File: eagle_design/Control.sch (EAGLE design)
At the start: 8 parts

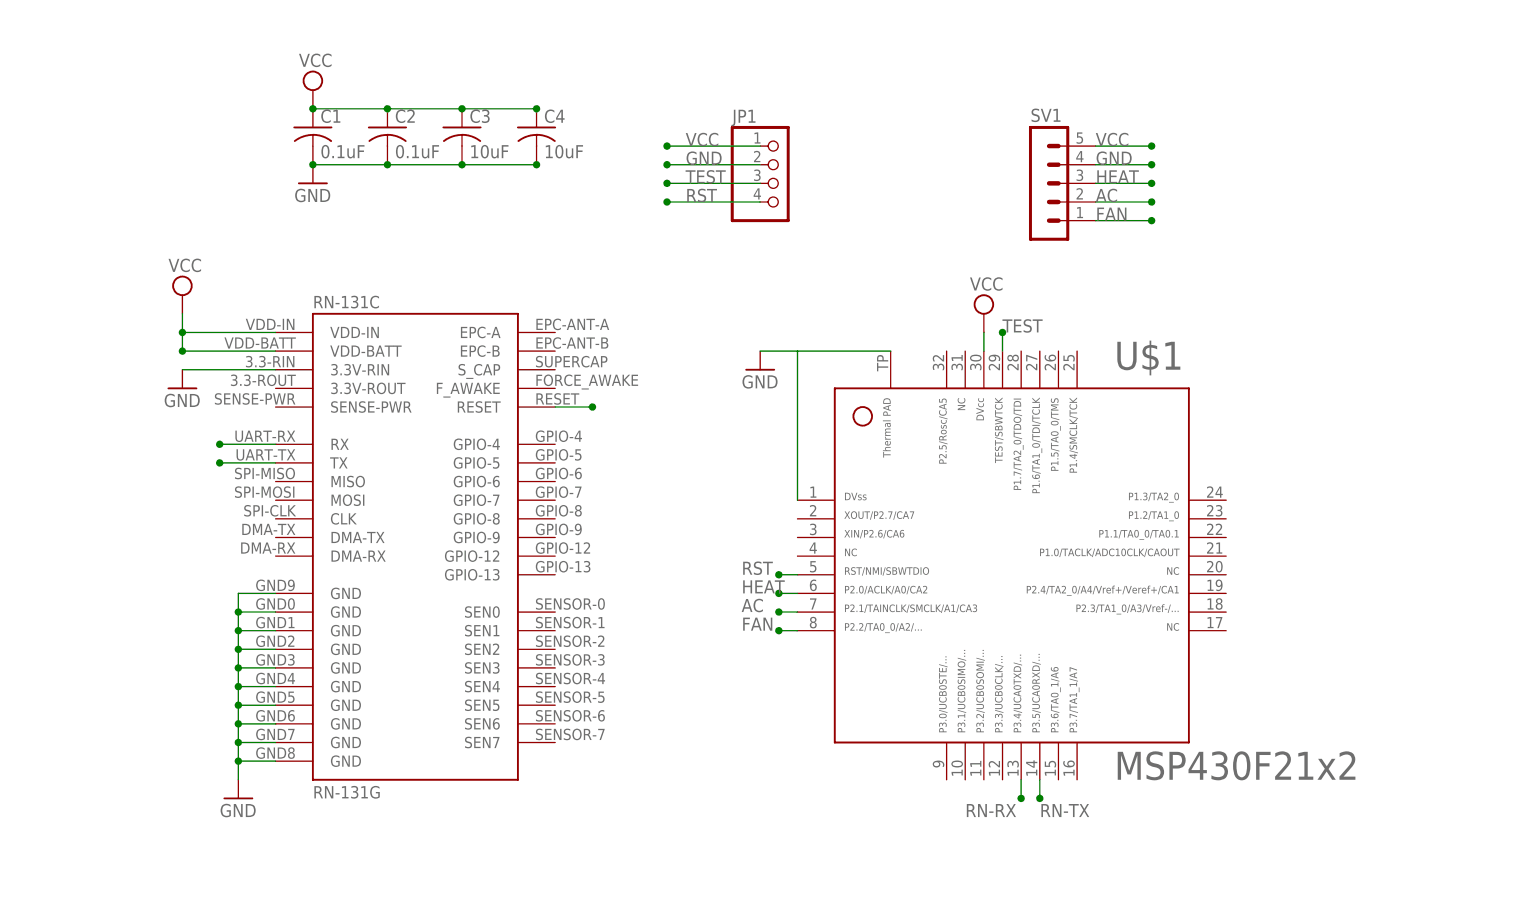
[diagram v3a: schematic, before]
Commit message: updated schematics
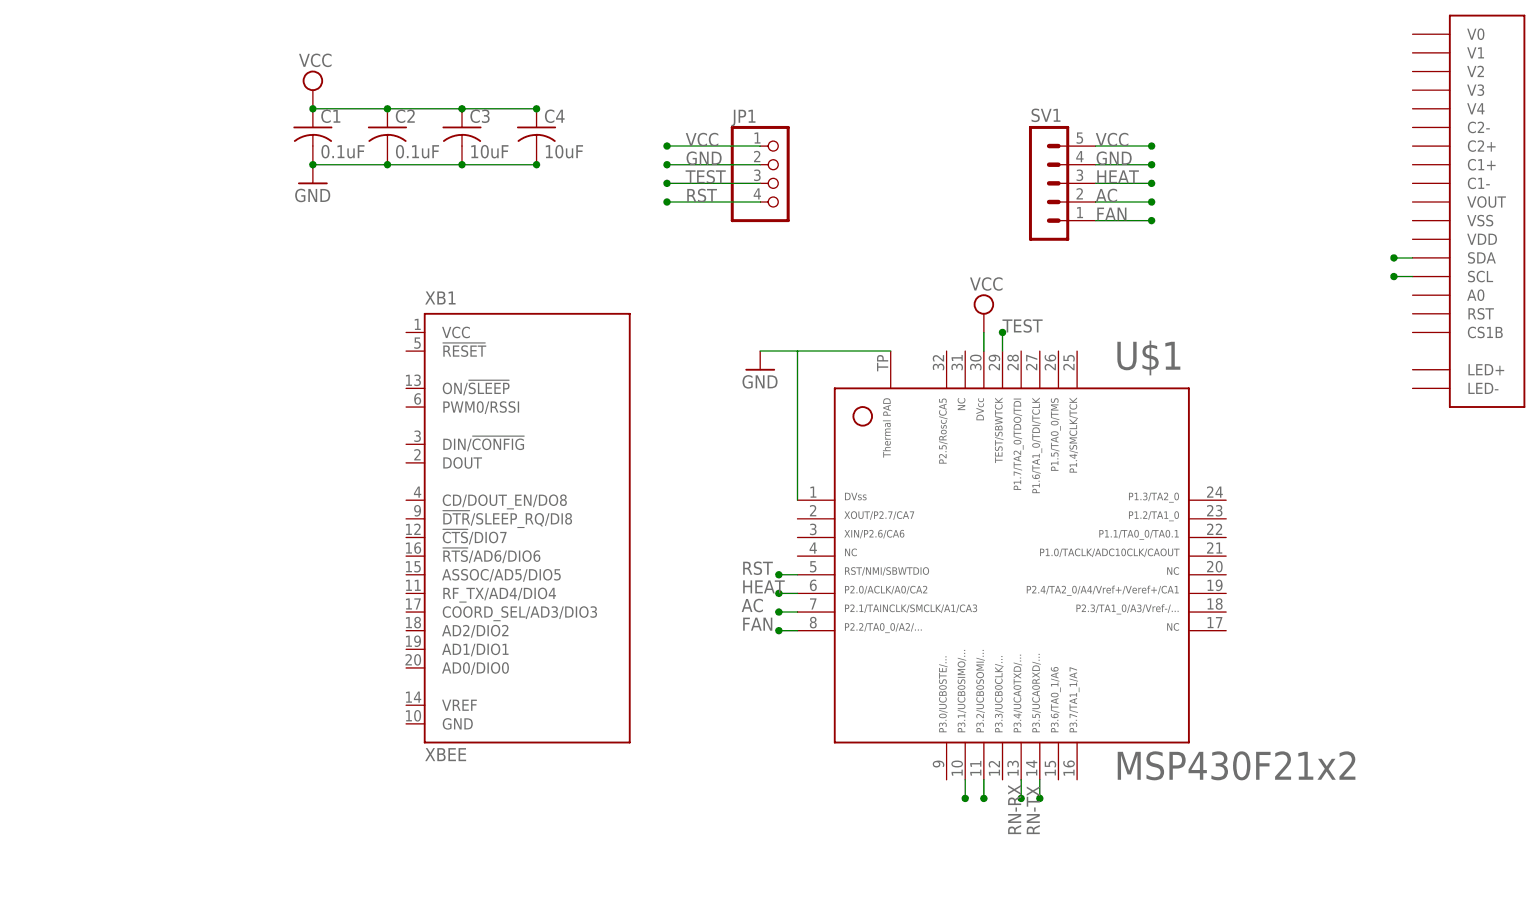
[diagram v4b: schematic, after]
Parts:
- removed RN-131C: RN-131G, SparkFun:RN-131G
- added U$2: NHD-C12832A1Z-FSW-FBW-3V3, TylersLib:NHD-C12832A1Z-FSW-FBW-3V3
- added XB1: XBEE, maxstream:XBEE
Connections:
- removed net RESET: RN-131C.RESET
- new net SCL: U$1.11, U$2.SCL
- new net SDA: U$1.10, U$2.SDA
- net GND: no longer RN-131C.3.3V-RIN, RN-131C.GND@19, RN-131C.GND@36, RN-131C.GND@37, RN-131C.GND@38, RN-131C.GND@39, RN-131C.GND@40, RN-131C.GND@41, RN-131C.GND@42, RN-131C.GND@43, RN-131C.GND@44
- net RN-RX: no longer RN-131C.RX
- net RN-TX: no longer RN-131C.TX
- net VCC: no longer RN-131C.VDD-BATT, RN-131C.VDD-IN
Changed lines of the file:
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@@
 </classes>
 <parts>
-<part name="GND1" library="supply1" deviceset="GND" device=""/>
-<part name="SUPPLY1" library="supply2" deviceset="VCC" device=""/>
-<part name="GND2" library="supply1" deviceset="GND" device=""/>
-<part name="RN-131C" library="SparkFun" deviceset="RN-131G" device=""/>
 <part name="SV1" library="con-lstb" deviceset="MA05-1" device=""/>
 <part name="C1" library="rcl" deviceset="C-US" device="C0805" value="0.1uF"/>
@@
 <part name="SUPPLY4" library="supply2" deviceset="VCC" device=""/>
 <part name="JP1" library="pinhead" deviceset="PINHD-1X4" device=""/>
+<part name="U$2" library="TylersLib" deviceset="NHD-C12832A1Z-FSW-FBW-3V3" device=""/>
+<part name="XB1" library="maxstream" deviceset="XBEE" device=""/>
 </parts>
 <sheets>
@@
 </plain>
 <instances>
-<instance part="GND1" gate="1" x="27.94" y="12.7"/>
-<instance part="SUPPLY1" gate="G$1" x="20.32" y="81.28"/>
-<instance part="GND2" gate="1" x="20.32" y="68.58"/>
-<instance part="RN-131C" gate="G$1" x="53.34" y="48.26"/>
 <instance part="SV1" gate="G$1" x="137.16" y="96.52"/>
 <instance part="C1" gate="G$1" x="38.1" y="104.14"/>
@@
 <instance part="SUPPLY4" gate="G$1" x="129.54" y="78.74"/>
 <instance part="JP1" gate="A" x="101.6" y="96.52"/>
+<instance part="U$2" gate="G$1" x="220.98" y="83.82"/>
+<instance part="XB1" gate="G$1" x="66.04" y="50.8"/>
 </instances>
 <busses>
@@
 <nets>
 <net name="VCC" class="0">
-<segment>
-<pinref part="SUPPLY1" gate="G$1" pin="VCC"/>
-<wire x1="20.32" y1="78.74" x2="20.32" y2="76.2" width="0.1524" layer="91"/>
-<junction x="20.32" y="73.66"/>
-<junction x="20.32" y="76.2"/>
-<wire x1="20.32" y1="76.2" x2="20.32" y2="73.66" width="0.1524" layer="91"/>
-<wire x1="33.02" y1="76.2" x2="20.32" y2="76.2" width="0.1524" layer="91"/>
-<wire x1="33.02" y1="73.66" x2="20.32" y2="73.66" width="0.1524" layer="91"/>
-<pinref part="RN-131C" gate="G$1" pin="VDD-BATT"/>
-<pinref part="RN-131C" gate="G$1" pin="VDD-IN"/>
-</segment>
 <segment>
 <pinref part="SV1" gate="G$1" pin="5"/>
@@
 <net name="RN-RX" class="0">
 <segment>
-<wire x1="33.02" y1="60.96" x2="25.4" y2="60.96" width="0.1524" layer="91"/>
-<pinref part="RN-131C" gate="G$1" pin="RX"/>
-<junction x="25.4" y="60.96"/>
-</segment>
-<segment>
 <pinref part="U$1" gate="G$1" pin="13"/>
 <wire x1="134.62" y1="15.24" x2="134.62" y2="12.7" width="0.1524" layer="91"/>
 <junction x="134.62" y="12.7"/>
-<label x="127" y="10.16" size="1.778" layer="95"/>
+<label x="134.62" y="7.62" size="1.778" layer="95" rot="R90"/>
 </segment>
 </net>
 <net name="RN-TX" class="0">
-<segment>
-<wire x1="33.02" y1="58.42" x2="25.4" y2="58.42" width="0.1524" layer="91"/>
-<pinref part="RN-131C" gate="G$1" pin="TX"/>
-<junction x="25.4" y="58.42"/>
-</segment>
 <segment>
 <pinref part="U$1" gate="G$1" pin="14"/>
 <wire x1="137.16" y1="15.24" x2="137.16" y2="12.7" width="0.1524" layer="91"/>
 <junction x="137.16" y="12.7"/>
-<label x="137.16" y="10.16" size="1.778" layer="95"/>
+<label x="137.16" y="7.62" size="1.778" layer="95" rot="R90"/>
 </segment>
 </net>
 <net name="GND" class="0">
-<segment>
-<wire x1="33.02" y1="40.64" x2="27.94" y2="40.64" width="0.1524" layer="91"/>
-<wire x1="27.94" y1="40.64" x2="27.94" y2="38.1" width="0.1524" layer="91"/>
-<junction x="27.94" y="38.1"/>
-<wire x1="27.94" y1="38.1" x2="27.94" y2="35.56" width="0.1524" layer="91"/>
-<junction x="27.94" y="35.56"/>
-<wire x1="27.94" y1="35.56" x2="27.94" y2="33.02" width="0.1524" layer="91"/>
-<junction x="27.94" y="33.02"/>
-<wire x1="27.94" y1="33.02" x2="27.94" y2="30.48" width="0.1524" layer="91"/>
-<junction x="27.94" y="30.48"/>
-<wire x1="27.94" y1="30.48" x2="27.94" y2="27.94" width="0.1524" layer="91"/>
-<junction x="27.94" y="27.94"/>
-<wire x1="27.94" y1="27.94" x2="27.94" y2="25.4" width="0.1524" layer="91"/>
-<junction x="27.94" y="25.4"/>
-<wire x1="27.94" y1="25.4" x2="27.94" y2="22.86" width="0.1524" layer="91"/>
-<junction x="27.94" y="22.86"/>
-<wire x1="27.94" y1="22.86" x2="27.94" y2="20.32" width="0.1524" layer="91"/>
-<junction x="27.94" y="20.32"/>
-<wire x1="27.94" y1="20.32" x2="27.94" y2="17.78" width="0.1524" layer="91"/>
-<wire x1="33.02" y1="17.78" x2="27.94" y2="17.78" width="0.1524" layer="91"/>
-<wire x1="33.02" y1="20.32" x2="27.94" y2="20.32" width="0.1524" layer="91"/>
-<wire x1="33.02" y1="22.86" x2="27.94" y2="22.86" width="0.1524" layer="91"/>
-<wire x1="33.02" y1="25.4" x2="27.94" y2="25.4" width="0.1524" layer="91"/>
-<wire x1="33.02" y1="27.94" x2="27.94" y2="27.94" width="0.1524" layer="91"/>
-<wire x1="33.02" y1="30.48" x2="27.94" y2="30.48" width="0.1524" layer="91"/>
-<wire x1="33.02" y1="33.02" x2="27.94" y2="33.02" width="0.1524" layer="91"/>
-<wire x1="33.02" y1="35.56" x2="27.94" y2="35.56" width="0.1524" layer="91"/>
-<wire x1="33.02" y1="38.1" x2="27.94" y2="38.1" width="0.1524" layer="91"/>
-<junction x="27.94" y="17.78"/>
-<pinref part="GND1" gate="1" pin="GND"/>
-<wire x1="27.94" y1="15.24" x2="27.94" y2="17.78" width="0.1524" layer="91"/>
-<pinref part="RN-131C" gate="G$1" pin="GND@19"/>
-<pinref part="RN-131C" gate="G$1" pin="GND@36"/>
-<pinref part="RN-131C" gate="G$1" pin="GND@37"/>
-<pinref part="RN-131C" gate="G$1" pin="GND@38"/>
-<pinref part="RN-131C" gate="G$1" pin="GND@39"/>
-<pinref part="RN-131C" gate="G$1" pin="GND@40"/>
-<pinref part="RN-131C" gate="G$1" pin="GND@41"/>
-<pinref part="RN-131C" gate="G$1" pin="GND@42"/>
-<pinref part="RN-131C" gate="G$1" pin="GND@43"/>
-<pinref part="RN-131C" gate="G$1" pin="GND@44"/>
-</segment>
-<segment>
-<pinref part="GND2" gate="1" pin="GND"/>
-<wire x1="20.32" y1="71.12" x2="33.02" y2="71.12" width="0.1524" layer="91"/>
-<pinref part="RN-131C" gate="G$1" pin="3.3V-RIN"/>
-</segment>
 <segment>
 <pinref part="SV1" gate="G$1" pin="4"/>
@@
 </segment>
 </net>
-<net name="RESET" class="0">
-<segment>
-<wire x1="71.12" y1="66.04" x2="76.2" y2="66.04" width="0.1524" layer="91"/>
-<pinref part="RN-131C" gate="G$1" pin="RESET"/>
-<junction x="76.2" y="66.04"/>
-</segment>
-</net>
 <net name="HEAT" class="0">
 <segment>
@@
 </segment>
 </net>
+<net name="SDA" class="0">
+<segment>
+<pinref part="U$1" gate="G$1" pin="10"/>
+<wire x1="127" y1="15.24" x2="127" y2="12.7" width="0.1524" layer="91"/>
+<junction x="127" y="12.7"/>
+</segment>
+<segment>
+<pinref part="U$2" gate="G$1" pin="SDA"/>
+<wire x1="187.96" y1="86.36" x2="185.42" y2="86.36" width="0.1524" layer="91"/>
+<junction x="185.42" y="86.36"/>
+</segment>
+</net>
+<net name="SCL" class="0">
+<segment>
+<pinref part="U$1" gate="G$1" pin="11"/>
+<wire x1="129.54" y1="15.24" x2="129.54" y2="12.7" width="0.1524" layer="91"/>
+<junction x="129.54" y="12.7"/>
+</segment>
+<segment>
+<pinref part="U$2" gate="G$1" pin="SCL"/>
+<wire x1="187.96" y1="83.82" x2="185.42" y2="83.82" width="0.1524" layer="91"/>
+<junction x="185.42" y="83.82"/>
+</segment>
+</net>

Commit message: added code, and modified eagle files
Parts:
- removed JP1: (no value), pinhead:PINHD-1X4
- removed XB1: XBEE, maxstream:XBEE
- added C10, C5, C6, C7, C8, C9: (no value), cap-pan40:C-NP-SMD-0603
- added R1: 100 kOhm, Panasonic_By_element14_Batch_1:ERA-3AEB104V
- added SPW: (no value), pinhead:PINHD-2X2
- added U$3: NHD-C12832A1Z-FSW-FBW-3V3, TylersLib:NHD-C12832A1Z-FSW-FBW-3V3
- added XB2: RN-XVB1, SteveMarple:RN-XVB1
- C1: device rcl:C-USC0805 -> rcl:C-USC0603K
- C2: value 0.1uF -> 10uF; device rcl:C-USC0805 -> rcl:C-USC0603K
- C3, C4: value 10uF -> (none); device rcl:C-USC0805 -> cap-pan40:C-NP-SMD-0603
- SV1: device con-lstb:MA05-1 -> con-lstb:MA03-1
- U$1: value F21X2---RHB32 -> G2XX3---PW28; device TI_MSP430_v16:F21X2---RHB32 -> TI_MSP430_v16:G2XX3---PW28
- U$2: value NHD-C12832A1Z-FSW-FBW-3V3 -> TEMPERATURE-SENSOR; device TylersLib:NHD-C12832A1Z-FSW-FBW-3V3 -> SparkFun-Sensors:TEMPERATURE-SENSOR
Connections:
- net RN-RX renamed P3_2
- net RN-TX renamed P3_3
- new net A0: U$1.8, U$3.A0
- new net CS: U$1.9, U$3.CS1B
- new net N$1: C3.2, U$3.V0
- new net N$10: C9.1, U$3.C1-
- new net N$11: R1.R1, U$3.LED+
- new net N$2: C4.2, U$3.V1
- new net N$3: C5.2, U$3.V2
- new net N$4: C6.2, U$3.V3
- new net N$5: C7.2, U$3.V4
- new net N$6: C8.2, U$3.C2-
- new net N$7: C9.2, U$3.C1+
- new net N$8: C8.1, U$3.C2+
- new net N$9: C10.2, U$3.VOUT
- new net P1_3: U$1.5
- new net P1_4: U$1.6
- new net P1_6: U$1.22
- new net P2_0: U$1.10
- new net P2_1: U$1.11
- new net P2_2: U$1.12
- new net P2_3: U$1.16
- new net P2_4: U$1.17
- new net P2_5: U$1.18
- new net P2_6: U$1.27
- new net P2_7: U$1.26
- new net P3_4: U$1.15
- new net P3_5: U$1.19
- new net P3_6: U$1.20
- new net P3_7: U$1.21
- new net RX: U$1.3, XB2.UART_TX
- new net TEMP: U$1.2, U$2.ADJ
- new net TX: U$1.4, XB2.UART_RX
- net AC: no longer U$1.7
- net FAN: now also SV1.3; no longer SV1.1, U$1.8
- net GND: now also C10.1, C3.1, C4.1, C5.1, C6.1, C7.1, SPW.3, U$1.28, U$2.GND, U$3.LED-, U$3.VSS, XB2.GND; no longer C3.2, C4.2, JP1.2, SV1.4, U$1.1, U$1.33
- net HEAT: now also SV1.1; no longer SV1.3, U$1.6
- net RST: now also SPW.4, U$1.24; no longer JP1.4, U$1.5
- net SCL: now also U$1.7, U$3.SCL; no longer U$1.11, U$2.SCL
- net SDA: now also U$1.23, U$3.SDA; no longer U$1.10, U$2.SDA
- net TEST: now also SPW.2, U$1.25; no longer JP1.3, U$1.29
- net VCC: now also R1.R2, SPW.1, U$1.1, U$2.VCC, U$3.RST, U$3.VDD, XB2.!RESET, XB2.VCC; no longer C3.1, C4.1, JP1.1, SV1.5, U$1.30
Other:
- moved on the sheet: C1, C2
